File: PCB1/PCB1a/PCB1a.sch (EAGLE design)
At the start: 0 parts

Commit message: ,,
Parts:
- added HUB08RG, HUB12RG, HUB75RGB, HUB75RGB.: 61231620621, Wurth_Connectors_WR-BHD:6123XX20621_61231620621
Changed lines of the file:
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@@
 <layer number="48" name="Document" color="7" fill="1" visible="no" active="no"/>
 <layer number="49" name="Reference" color="7" fill="1" visible="no" active="no"/>
+<layer number="50" name="dxf" color="7" fill="1" visible="no" active="no"/>
 <layer number="51" name="tDocu" color="7" fill="1" visible="no" active="no"/>
 <layer number="52" name="bDocu" color="7" fill="1" visible="no" active="no"/>
@@
 <layer number="97" name="Info" color="7" fill="1" visible="yes" active="yes"/>
 <layer number="98" name="Guide" color="6" fill="1" visible="yes" active="yes"/>
+<layer number="250" name="Descript" color="7" fill="1" visible="yes" active="yes"/>
+<layer number="251" name="SMDround" color="7" fill="1" visible="yes" active="yes"/>
 </layers>
 <schematic xreflabel="%F%N/%S.%C%R" xrefpart="/%S.%C%R">
@@
 <parts>
 <part name="GND1" library="supply1" library_urn="urn:adsk.eagle:library:371" deviceset="GND" device=""/>
+<part name="HUB75RGB" library="Wurth_Connectors_WR-BHD" library_urn="urn:adsk.eagle:library:15268170" deviceset="6123XX20621_61231620621" device="" package3d_urn="urn:adsk.eagle:package:15268446/6" value=" 61231620621 "/>
+<part name="HUB75RGB." library="Wurth_Connectors_WR-BHD" library_urn="urn:adsk.eagle:library:15268170" deviceset="6123XX20621_61231620621" device="" package3d_urn="urn:adsk.eagle:package:15268446/6" value=" 61231620621 "/>
+<part name="HUB08RG" library="Wurth_Connectors_WR-BHD" library_urn="urn:adsk.eagle:library:15268170" deviceset="6123XX20621_61231620621" device="" package3d_urn="urn:adsk.eagle:package:15268446/6" value=" 61231620621 "/>
+<part name="HUB12RG" library="Wurth_Connectors_WR-BHD" library_urn="urn:adsk.eagle:library:15268170" deviceset="6123XX20621_61231620621" device="" package3d_urn="urn:adsk.eagle:package:15268446/6" value=" 61231620621 "/>
 </parts>
 <sheets>
@@
 <instance part="GND1" gate="1" x="12.7" y="12.7" smashed="yes">
 <attribute name="VALUE" x="10.16" y="10.16" size="1.778" layer="96"/>
+</instance>
+<instance part="HUB75RGB" gate="G$1" x="33.02" y="116.84" smashed="yes" rot="R90">
+<attribute name="NAME" x="32.452" y="106.986" size="1.016" layer="95" rot="R90" align="bottom-right"/>
+<attribute name="VALUE" x="34.504" y="106.862" size="1.016" layer="96" rot="R90" align="bottom-right"/>
+</instance>
+<instance part="HUB75RGB." gate="G$1" x="33.02" y="53.34" smashed="yes" rot="R90">
+<attribute name="NAME" x="32.452" y="43.486" size="1.016" layer="95" rot="R90" align="bottom-right"/>
+<attribute name="VALUE" x="34.504" y="43.362" size="1.016" layer="96" rot="R90" align="bottom-right"/>
+</instance>
+<instance part="HUB08RG" gate="G$1" x="33.02" y="83.82" smashed="yes" rot="R90">
+<attribute name="NAME" x="32.452" y="73.966" size="1.016" layer="95" rot="R90" align="bottom-right"/>
+<attribute name="VALUE" x="34.504" y="73.842" size="1.016" layer="96" rot="R90" align="bottom-right"/>
+</instance>
+<instance part="HUB12RG" gate="G$1" x="33.02" y="22.86" smashed="yes" rot="R90">
+<attribute name="NAME" x="32.452" y="13.006" size="1.016" layer="95" rot="R90" align="bottom-right"/>
+<attribute name="VALUE" x="34.504" y="12.882" size="1.016" layer="96" rot="R90" align="bottom-right"/>
 </instance>
 </instances>
@@
 will not be understood (or retained) with this version.
 </note>
+<note version="8.3" severity="warning">
+Since Version 8.3, EAGLE supports the association of 3D packages
+with devices in libraries, schematics, and board files. Those 3D
+packages will not be understood (or retained) with this version.
+</note>
 </compatibility>

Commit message: .
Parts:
- added J1: 691318400002, Wurth_Connectors_WR-TBL Pluggable Connector:691318400002
- added J2: 691317410002, Wurth_Connectors_WR-TBL Pluggable Connector:691317410002
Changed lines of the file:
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@@
 <part name="HUB08RG" library="Wurth_Connectors_WR-BHD" library_urn="urn:adsk.eagle:library:15268170" deviceset="6123XX20621_61231620621" device="" package3d_urn="urn:adsk.eagle:package:15268446/6" value=" 61231620621 "/>
 <part name="HUB12RG" library="Wurth_Connectors_WR-BHD" library_urn="urn:adsk.eagle:library:15268170" deviceset="6123XX20621_61231620621" device="" package3d_urn="urn:adsk.eagle:package:15268446/6" value=" 61231620621 "/>
+<part name="J1" library="Wurth_Connectors_WR-TBL Pluggable Connector" library_urn="urn:adsk.eagle:library:16280984" deviceset="691318400002" device="" package3d_urn="urn:adsk.eagle:package:16282433/2" value=" 691318400002 "/>
+<part name="J2" library="Wurth_Connectors_WR-TBL Pluggable Connector" library_urn="urn:adsk.eagle:library:16280984" deviceset="691317410002" device="" package3d_urn="urn:adsk.eagle:package:16282458/2" value=" 691317410002 "/>
 </parts>
 <sheets>
@@
 <attribute name="VALUE" x="34.504" y="12.882" size="1.016" layer="96" rot="R90" align="bottom-right"/>
 </instance>
+<instance part="J1" gate="G$1" x="50.8" y="165.1" smashed="yes">
+<attribute name="NAME" x="45.81" y="163.895" size="1.016" layer="95" align="bottom-right"/>
+<attribute name="VALUE" x="45.85" y="162.09" size="1.016" layer="96" align="bottom-right"/>
+</instance>
+<instance part="J2" gate="G$1" x="-96.52" y="251.46" smashed="yes">
+<attribute name="NAME" x="-101.51" y="250.255" size="1.016" layer="95" align="bottom-right"/>
+<attribute name="VALUE" x="-101.47" y="248.45" size="1.016" layer="96" align="bottom-right"/>
+</instance>
 </instances>

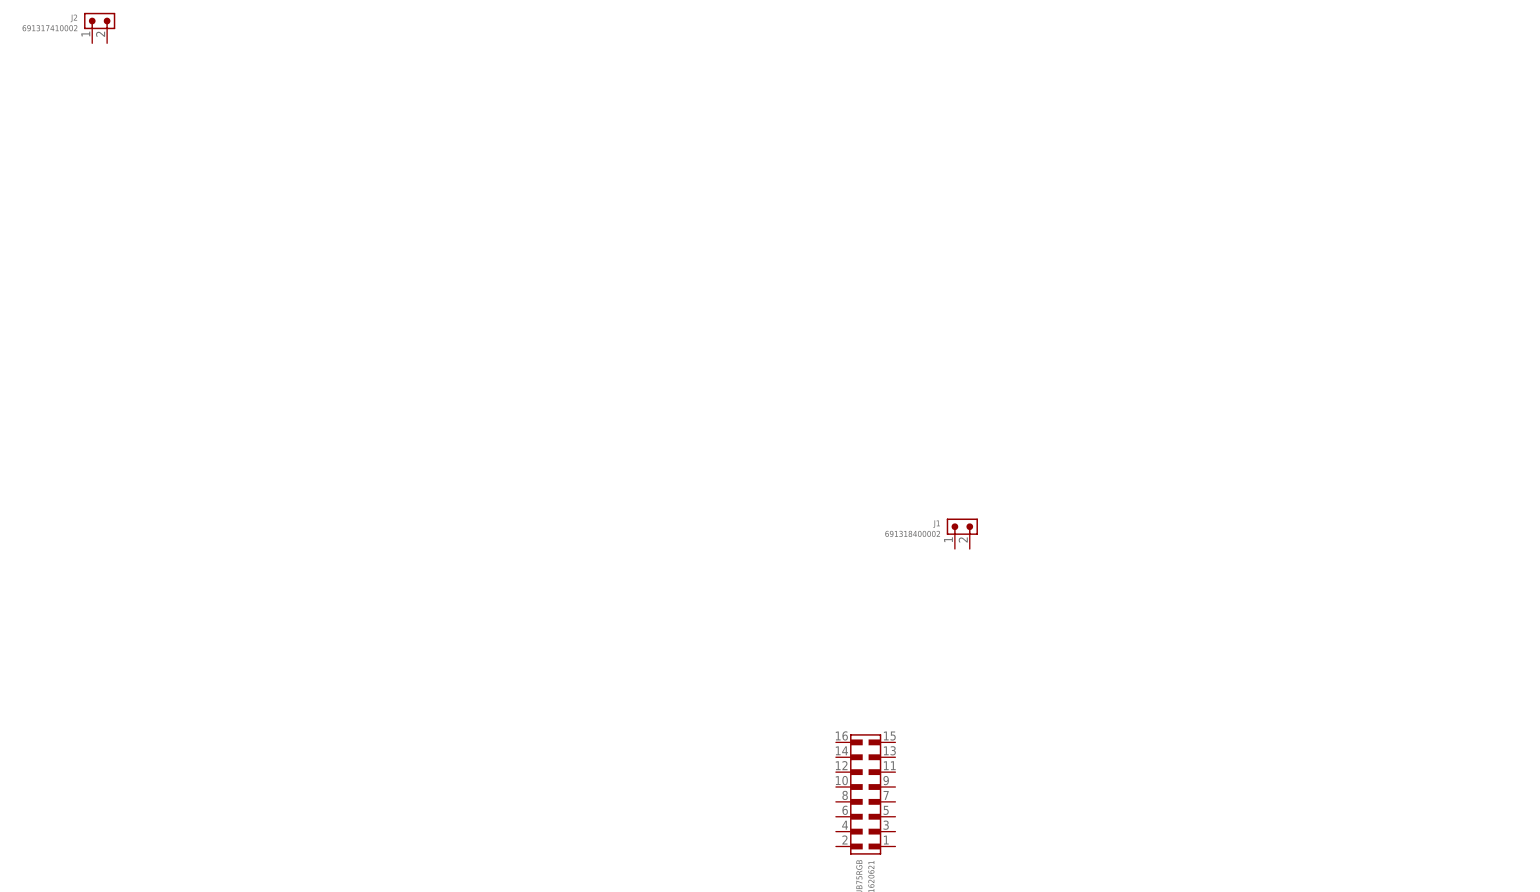
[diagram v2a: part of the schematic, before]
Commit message: power Conn. added.
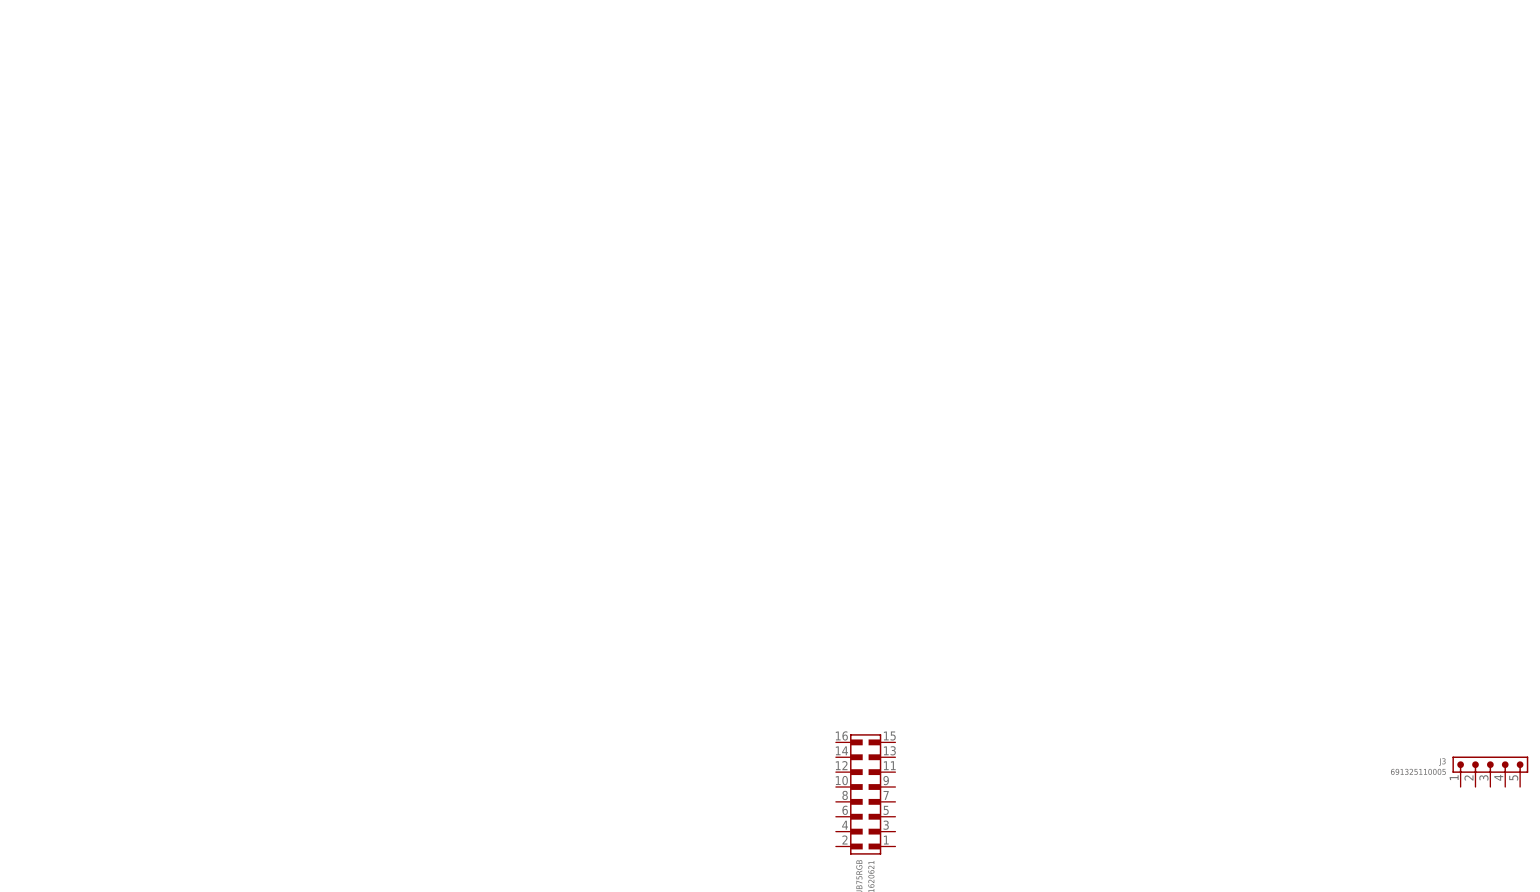
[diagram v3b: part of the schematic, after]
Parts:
- removed J1: 691318400002, Wurth_Connectors_WR-TBL Pluggable Connector:691318400002
- removed J2: 691317410002, Wurth_Connectors_WR-TBL Pluggable Connector:691317410002
- added J3: 691325110005, Wurth_Connectors_WR-TBL Pluggable Connector:691325110005
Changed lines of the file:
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@@
 <part name="HUB08RG" library="Wurth_Connectors_WR-BHD" library_urn="urn:adsk.eagle:library:15268170" deviceset="6123XX20621_61231620621" device="" package3d_urn="urn:adsk.eagle:package:15268446/6" value=" 61231620621 "/>
 <part name="HUB12RG" library="Wurth_Connectors_WR-BHD" library_urn="urn:adsk.eagle:library:15268170" deviceset="6123XX20621_61231620621" device="" package3d_urn="urn:adsk.eagle:package:15268446/6" value=" 61231620621 "/>
-<part name="J1" library="Wurth_Connectors_WR-TBL Pluggable Connector" library_urn="urn:adsk.eagle:library:16280984" deviceset="691318400002" device="" package3d_urn="urn:adsk.eagle:package:16282433/2" value=" 691318400002 "/>
-<part name="J2" library="Wurth_Connectors_WR-TBL Pluggable Connector" library_urn="urn:adsk.eagle:library:16280984" deviceset="691317410002" device="" package3d_urn="urn:adsk.eagle:package:16282458/2" value=" 691317410002 "/>
+<part name="J3" library="Wurth_Connectors_WR-TBL Pluggable Connector" library_urn="urn:adsk.eagle:library:16280984" deviceset="691325110005" device="" package3d_urn="urn:adsk.eagle:package:16281816/2" value=" 691325110005 "/>
 </parts>
 <sheets>
@@
 <attribute name="VALUE" x="34.504" y="12.882" size="1.016" layer="96" rot="R90" align="bottom-right"/>
 </instance>
-<instance part="J1" gate="G$1" x="50.8" y="165.1" smashed="yes">
-<attribute name="NAME" x="45.81" y="163.895" size="1.016" layer="95" align="bottom-right"/>
-<attribute name="VALUE" x="45.85" y="162.09" size="1.016" layer="96" align="bottom-right"/>
-</instance>
-<instance part="J2" gate="G$1" x="-96.52" y="251.46" smashed="yes">
-<attribute name="NAME" x="-101.51" y="250.255" size="1.016" layer="95" align="bottom-right"/>
-<attribute name="VALUE" x="-101.47" y="248.45" size="1.016" layer="96" align="bottom-right"/>
+<instance part="J3" gate="G$1" x="139.7" y="124.46" smashed="yes">
+<attribute name="NAME" x="132.17" y="123.255" size="1.016" layer="95" align="bottom-right"/>
+<attribute name="VALUE" x="132.21" y="121.45" size="1.016" layer="96" align="bottom-right"/>
 </instance>
 </instances>

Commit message: -
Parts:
- removed J3: 691325110005, Wurth_Connectors_WR-TBL Pluggable Connector:691325110005
- added J1: 691357310006B, Wurth_Connectors_WR-TBL Pluggable Connector:691357310006B
- added U8, U9: 74AHCT245, microbuilder:74LCX245_TSSOP20
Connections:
- new net +5V: U8.T/R, U8.VCC, U9.T/R, U9.VCC
- new net ADDRA_3V: U8.A4
- new net ADDRB_3V: U9.A8
- new net ADDRC_3V: U8.A5
- new net ADDRD_3V: U8.A3
- new net ADDRE_3V: U8.A7
- new net B1_3V: U9.A3
- new net B2_3V: U9.A6
- new net CLK_3V: U9.A7
- new net G1_3V: U9.A2
- new net G2_3V: U9.A4
- new net GND: HUB08RG.1, HUB08RG.13, HUB08RG.15, HUB08RG.3, HUB08RG.5, HUB12RG.11, HUB12RG.13, HUB12RG.15, HUB12RG.3, HUB12RG.5, HUB12RG.7, HUB12RG.9, HUB75RGB..16, HUB75RGB..4, HUB75RGB..8, HUB75RGB.16, HUB75RGB.4, HUB75RGB.8, U8./OE, U8.A1, U8.A2, U8.GND, U9./OE, U9.GND
- new net LAT_3V: U8.A6
- new net M1_A: HUB08RG.2, HUB12RG.2, HUB75RGB..9, HUB75RGB.9, U8.B4
- new net M1_B: HUB08RG.4, HUB12RG.4, HUB75RGB..10, HUB75RGB.10, U9.B8
- new net M1_B1: HUB75RGB..3, HUB75RGB.3, U9.B3
- new net M1_B2: HUB75RGB..7, HUB75RGB.7, U9.B6
- new net M1_C: HUB08RG.6, HUB12RG.6, HUB75RGB..11, HUB75RGB.11, U8.B5
- new net M1_CLK: HUB08RG.16, HUB12RG.8, HUB75RGB..13, HUB75RGB.13, U9.B7
- new net M1_D: HUB08RG.8, HUB12RG.16, HUB75RGB..12, HUB75RGB.12, U8.B3
- new net M1_E: U8.B7
- new net M1_G1: HUB08RG.10, HUB12RG.14, HUB75RGB..2, HUB75RGB.2, U9.B2
- new net M1_G2: HUB08RG.12, HUB75RGB..6, HUB75RGB.6, U9.B4
- new net M1_LAT: HUB08RG.14, HUB12RG.10, HUB75RGB..14, HUB75RGB.14, U8.B6
- new net M1_OE: HUB08RG.7, HUB12RG.1, HUB75RGB..15, HUB75RGB.15, U8.B8
- new net M1_R1: HUB08RG.9, HUB12RG.12, HUB75RGB..1, HUB75RGB.1, U9.B1
- new net M1_R2: HUB08RG.11, HUB75RGB..5, HUB75RGB.5, U9.B5
- new net OE_3V: U8.A8
- new net R1_3V: U9.A1
- new net R2_3V: U9.A5
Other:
- note added: "LEVEL SHIFTERS"
- moved on the sheet: HUB08RG, HUB12RG, HUB75RGB, HUB75RGB.

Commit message: ..
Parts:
- added J2: 618009231421, Wurth_Connectors_WR-DSUB:6180XX231421_618009231421
- added T1: 7498011211, Wurth_Signal & Communications_WE-RJ45_LAN:WE-RJ45_7498011211
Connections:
- new net CAN_H: J1.6
- new net CAN_L: J1.5
- new net RX: J2.2
- new net TX: J2.3
- net +5V: now also J1.3
- net GND: now also J1.1, J1.4, J2.5, J2.SHIELD
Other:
- moved on the sheet: J1
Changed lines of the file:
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@@
 <setting verticaltext="up"/>
 </settings>
-<grid distance="0.05" unitdist="inch" unit="inch" style="lines" multiple="1" display="no" altdistance="0.01" altunitdist="inch" altunit="inch"/>
+<grid distance="0.1" unitdist="inch" unit="inch" style="lines" multiple="1" display="yes" altdistance="0.01" altunitdist="inch" altunit="inch"/>
 <layers>
 <layer number="1" name="Top" color="4" fill="1" visible="no" active="no"/>
@@
 <part name="GND17" library="supply1" library_urn="urn:adsk.eagle:library:371" deviceset="GND" device=""/>
 <part name="GND18" library="supply1" library_urn="urn:adsk.eagle:library:371" deviceset="GND" device=""/>
+<part name="U$1" library="microbuilder" deviceset="GND" device=""/>
+<part name="J2" library="Wurth_Connectors_WR-DSUB" library_urn="urn:adsk.eagle:library:16444967" deviceset="6180XX231421_618009231421" device="" package3d_urn="urn:adsk.eagle:package:16445076/3" value="618009231421"/>
+<part name="GND19" library="supply1" library_urn="urn:adsk.eagle:library:371" deviceset="GND" device=""/>
+<part name="GND20" library="supply1" library_urn="urn:adsk.eagle:library:371" deviceset="GND" device=""/>
+<part name="T1" library="Wurth_Signal &amp; Communications_WE-RJ45_LAN" library_urn="urn:adsk.eagle:library:14284239" deviceset="WE-RJ45_7498011211" device="" package3d_urn="urn:adsk.eagle:package:12863525/4" value=" 7498011211 "/>
 </parts>
 <sheets>
@@
 <attribute name="VALUE" x="138.176" y="134.62" size="1.27" layer="96"/>
 </instance>
-<instance part="P+10" gate="1" x="147.32" y="137.16" smashed="yes" rot="R180">
-<attribute name="VALUE" x="149.86" y="137.16" size="1.778" layer="96" rot="R180"/>
+<instance part="P+10" gate="1" x="139.7" y="166.37" smashed="yes">
+<attribute name="VALUE" x="137.16" y="166.37" size="1.778" layer="96"/>
 </instance>
 <instance part="GND45" gate="1" x="129.54" y="76.2" smashed="yes" rot="R90">
@@
 <attribute name="VALUE" x="54.61" y="-8.89" size="1.778" layer="96" rot="R270"/>
 </instance>
-<instance part="J1" gate="G$1" x="21.59" y="-3.81" smashed="yes">
-<attribute name="NAME" x="15.33" y="-3.46" size="1.016" layer="95" align="bottom-right"/>
-<attribute name="VALUE" x="15.47" y="-5.68" size="1.016" layer="96" align="bottom-right"/>
+<instance part="J1" gate="G$1" x="127" y="152.4" smashed="yes" rot="R90">
+<attribute name="NAME" x="126.65" y="146.14" size="1.016" layer="95" rot="R90" align="bottom-right"/>
+<attribute name="VALUE" x="128.87" y="146.28" size="1.016" layer="96" rot="R90" align="bottom-right"/>
 </instance>
 <instance part="GND12" gate="1" x="57.15" y="-31.75" smashed="yes" rot="R270">
@@
 <instance part="GND18" gate="1" x="60.96" y="-44.45" smashed="yes" rot="R270">
 <attribute name="VALUE" x="58.42" y="-41.91" size="1.778" layer="96" rot="R270"/>
+</instance>
+<instance part="U$1" gate="G$1" x="114.3" y="137.16" smashed="yes">
+<attribute name="VALUE" x="112.776" y="134.62" size="1.27" layer="96"/>
+</instance>
+<instance part="J2" gate="G$1" x="91.44" y="-99.06" smashed="yes" rot="R90">
+<attribute name="NAME" x="89.78" y="-85.28" size="1.27" layer="95" rot="R90"/>
+<attribute name="VALUE" x="92.32" y="-85.18" size="1.27" layer="96" rot="R90"/>
+</instance>
+<instance part="GND19" gate="1" x="120.65" y="-95.25" smashed="yes">
+<attribute name="VALUE" x="118.11" y="-97.79" size="1.778" layer="96"/>
+</instance>
+<instance part="GND20" gate="1" x="71.12" y="-91.44" smashed="yes">
+<attribute name="VALUE" x="68.58" y="-93.98" size="1.778" layer="96"/>
+</instance>
+<instance part="T1" gate="G$1" x="340.36" y="-63.5" smashed="yes">
+<attribute name="NAME" x="340.36" y="-48.26" size="1.778" layer="95" align="bottom-center"/>
+<attribute name="VALUE" x="340.36" y="-83.82" size="1.778" layer="96" align="bottom-center"/>
+<attribute name="NAME" x="340.36" y="-48.26" size="1.778" layer="95" align="bottom-center"/>
 </instance>
 </instances>
@@
 <junction x="243.84" y="68.58"/>
 </segment>
+<segment>
+<pinref part="J1" gate="G$1" pin="3"/>
+<pinref part="P+10" gate="1" pin="+5V"/>
+<wire x1="132.08" y1="154.94" x2="139.7" y2="154.94" width="0.1524" layer="91"/>
+<wire x1="139.7" y1="154.94" x2="139.7" y2="163.83" width="0.1524" layer="91"/>
+</segment>
 </net>
 <net name="GND" class="0">
@@
 <pinref part="GND15" gate="1" pin="GND"/>
 </segment>
+<segment>
+<pinref part="J1" gate="G$1" pin="1"/>
+<pinref part="U$58" gate="G$1" pin="GND"/>
+<wire x1="132.08" y1="149.86" x2="139.7" y2="149.86" width="0.1524" layer="91"/>
+<wire x1="139.7" y1="149.86" x2="139.7" y2="139.7" width="0.1524" layer="91"/>
+</segment>
+<segment>
+<pinref part="J1" gate="G$1" pin="4"/>
+<pinref part="U$1" gate="G$1" pin="GND"/>
+<wire x1="121.92" y1="149.86" x2="114.3" y2="149.86" width="0.1524" layer="91"/>
+<wire x1="114.3" y1="149.86" x2="114.3" y2="139.7" width="0.1524" layer="91"/>
+</segment>
+<segment>
+<pinref part="GND19" gate="1" pin="GND"/>
+<pinref part="J2" gate="G$1" pin="SHIELD"/>
+<wire x1="120.65" y1="-92.71" x2="120.65" y2="-88.9" width="0.1524" layer="91"/>
+<wire x1="120.65" y1="-88.9" x2="99.06" y2="-88.9" width="0.1524" layer="91"/>
+</segment>
+<segment>
+<pinref part="J2" gate="G$1" pin="5"/>
+<wire x1="83.82" y1="-88.9" x2="71.12" y2="-88.9" width="0.1524" layer="91"/>
+<pinref part="GND20" gate="1" pin="GND"/>
+</segment>
 </net>
 <net name="OE_3V" class="0">
@@
 </segment>
 </net>
+<net name="RX" class="0">
+<segment>
+<pinref part="J2" gate="G$1" pin="2"/>
+<wire x1="83.82" y1="-104.14" x2="63.5" y2="-104.14" width="0.1524" layer="91"/>
+<label x="63.5" y="-104.14" size="1.778" layer="95"/>
+</segment>
+</net>
+<net name="TX" class="0">
+<segment>
+<pinref part="J2" gate="G$1" pin="3"/>
+<wire x1="83.82" y1="-99.06" x2="63.5" y2="-99.06" width="0.1524" layer="91"/>
+<label x="63.5" y="-99.06" size="1.778" layer="95"/>
+</segment>
+</net>
+<net name="CAN_H" class="0">
+<segment>
+<pinref part="J1" gate="G$1" pin="6"/>
+<wire x1="121.92" y1="154.94" x2="104.14" y2="154.94" width="0.1524" layer="91"/>
+<label x="104.14" y="154.94" size="1.778" layer="95"/>
+</segment>
+</net>
+<net name="CAN_L" class="0">
+<segment>
+<pinref part="J1" gate="G$1" pin="5"/>
+<wire x1="121.92" y1="152.4" x2="104.14" y2="152.4" width="0.1524" layer="91"/>
+<label x="104.14" y="152.4" size="1.778" layer="95"/>
+</segment>
+</net>
